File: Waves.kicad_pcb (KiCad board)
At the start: 2 copper layers, 49.8 x 106.5 mm, 154 parts, among them J1 AudioJack2_SwitchT, J10 AudioJack2_SwitchT, J11 Conn_01x04_Male, J12 Conn_01x04_Male, J13 AudioJack2_SwitchT, J14 AudioJack2_SwitchT, J15 Conn_02x05_Odd_Even, J2 AudioJack2_SwitchT, J3 AudioJack2_SwitchT, J4 AudioJack2_SwitchT, J5 AudioJack2_SwitchT, J6 AudioJack2_SwitchT, J7 AudioJack2_SwitchT, J8 AudioJack2_SwitchT, J9 AudioJack2_SwitchT, Q1 BC847, Q2 BC847, Q3 BC847, Q4 BC847, Q5 BC847, Q6 BC847, SW1 SW_Push, SW2 Rotary_Encoder_Switch, SW3 SW_Push_LED, SW4 SW_Push_LED, SW5 SW_Push_LED, SW6 SW_Push_LED, U1 STM32G431, U2 AT25xxx, U3 IPS240x240, U4 PCM5100, U5 TL072, U6 LM1117-3.3, U7 LM1117-3.3, U8 MCP6004, U9 MCP6004, Y1 8MHz

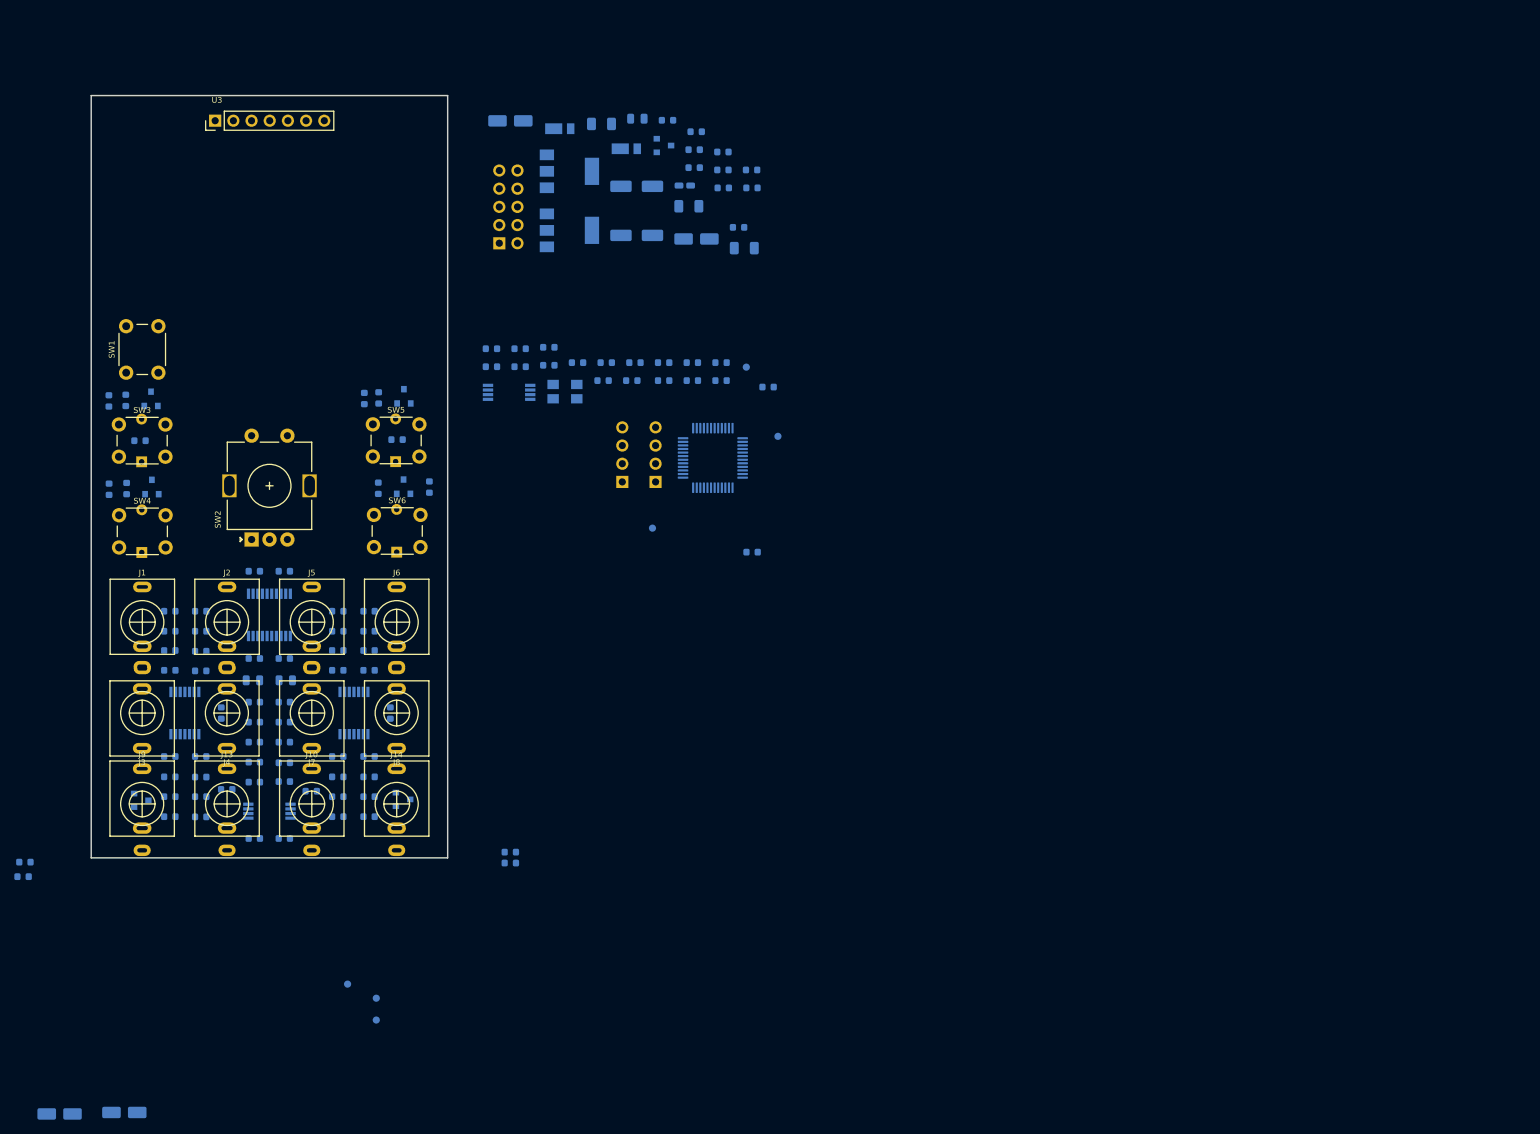
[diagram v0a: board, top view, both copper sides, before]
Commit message: Changed regulators and laid out power components.
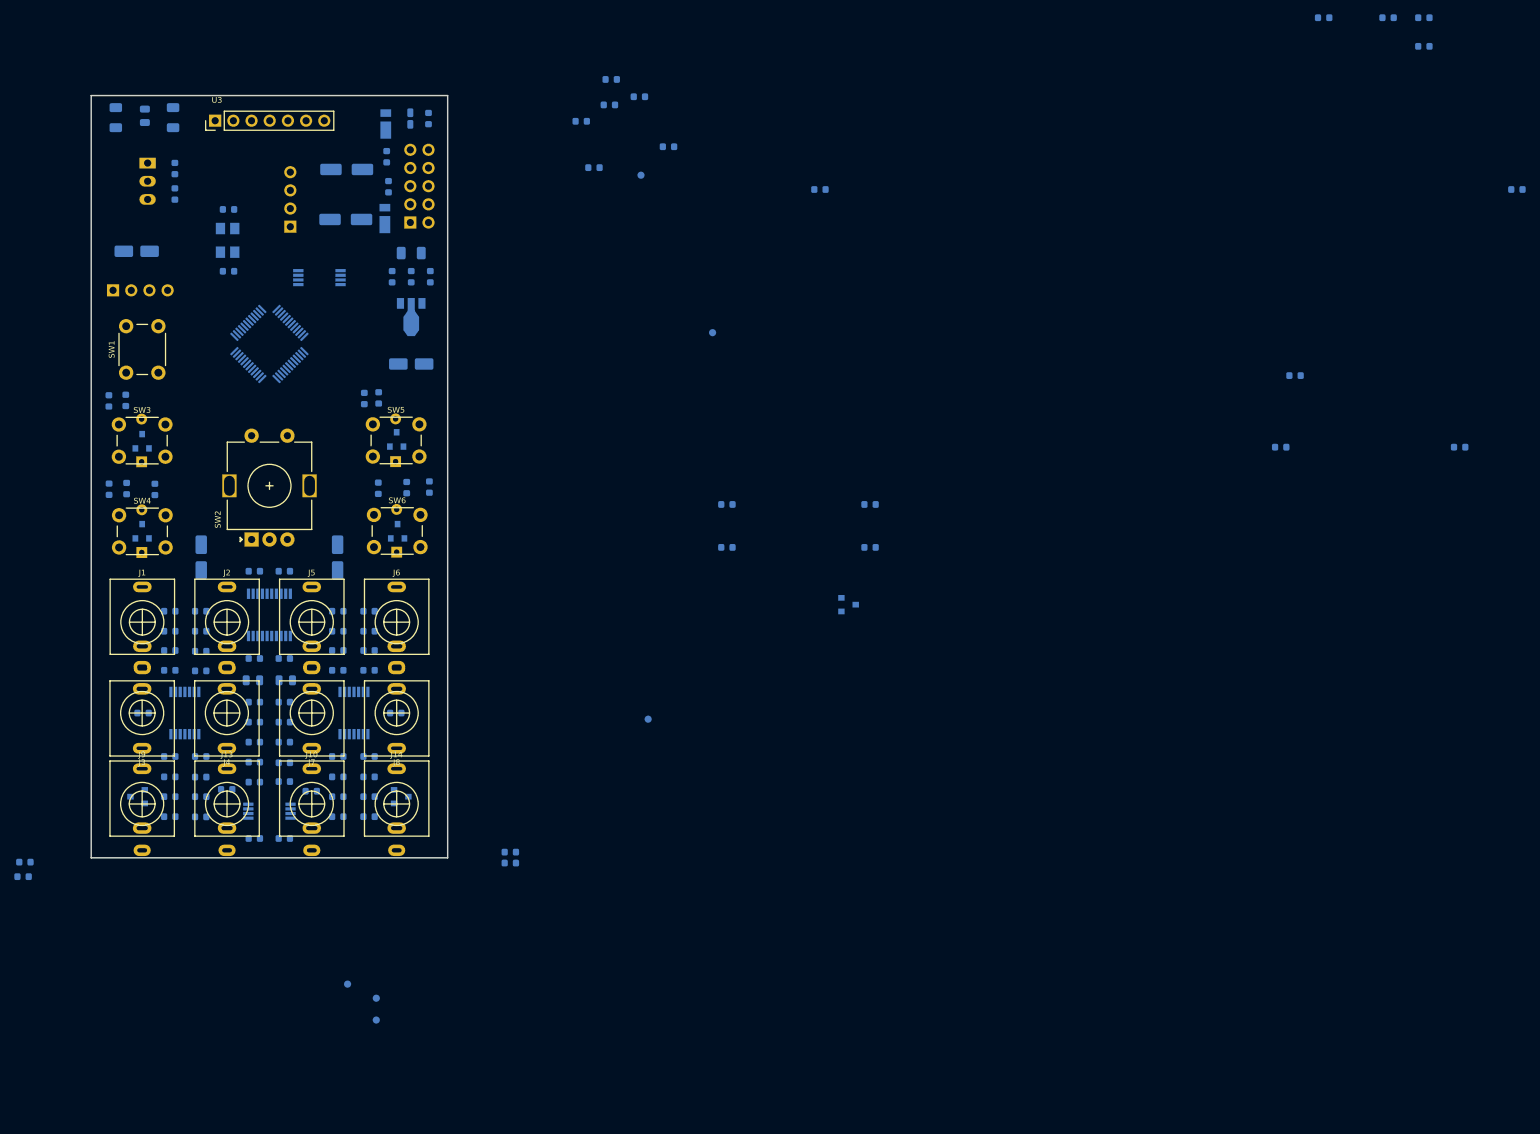
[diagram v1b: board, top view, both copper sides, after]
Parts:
- U6: value LM1117-3.3 -> R-78E3.3-0.5; footprint Package_TO_SOT_SMD:SOT-223-3_TabPin2 -> Converter_DCDC:Converter_DCDC_RECOM_R-78E-0.5_THT
- U7: value LM1117-3.3 -> LD2981ABU33TR; footprint Package_TO_SOT_SMD:SOT-223-3_TabPin2 -> Package_TO_SOT_SMD:SOT-89-3
- moved C13 126.1 mm to (274.2, 37.5)
- moved R6 121.6 mm to (301.2, 61.5)
- moved R4 113.0 mm to (288.2, 37.5)
- moved R3 108.7 mm to (288.2, 41.5)
- moved C42 105.3 mm to (293.2, 97.5)
- moved R9 104.9 mm to (283.2, 37.5)
- moved R19 87.0 mm to (268.2, 97.5)
- moved C17 83.0 mm to (136.4, 112.9), turned to 90 degrees
- moved C22 80.2 mm to (117.3, 112.9), turned to 90 degrees
- moved R5 79.8 mm to (270.2, 87.5)
- moved C40 78.2 mm to (108.3, 70.1), turned to 180 degrees
- moved J11 76.0 mm to (105.0, 75.6), turned to 270 degrees
- moved C31 73.1 mm to (113.4, 51.4), turned to 270 degrees
- moved C36 73.0 mm to (113.7, 58.5), turned to 270 degrees
- moved C38 69.6 mm to (113.7, 62.1), turned to 90 degrees
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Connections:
- U6 pad 1: GND -> Net-(C34-Pad1)
- U6 pad 2: +3V3 -> GND
- U6 pad 3: Net-(C34-Pad1) -> +3V3
- U7 pad 1: GND -> +3.3VA
- U7 pad 2: +3.3VA -> GND

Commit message: First pass complete layout.
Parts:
- removed TP4, TP5, TP6: TestPoint, TestPoint:TestPoint_Pad_D1.0mm
- moved R6 185.1 mm to (117.4, 84.3), turned to 180 degrees
- moved R4 174.1 mm to (116.6, 67.1), turned to 90 degrees
- moved R3 172.4 mm to (116.6, 58.7), turned to 90 degrees
- moved R5 161.1 mm to (109.1, 82.7)
- moved C13 158.9 mm to (124.0, 89.2), turned to 180 degrees
- moved C42 157.4 mm to (135.9, 91.4)
- moved R9 157.2 mm to (127.0, 55.5), turned to 270 degrees
- moved R19 132.3 mm to (135.9, 94.2), turned to 180 degrees
- moved C15 98.8 mm to (117.5, 78.9), turned to 180 degrees
- moved C16 97.8 mm to (117.5, 76.1), turned to 180 degrees
- moved C4 84.2 mm to (109.1, 85.1), turned to 180 degrees
- moved C14 79.1 mm to (124.7, 63.8), turned to 90 degrees
- moved D4 78.6 mm to (135.9, 87.6), turned to 90 degrees
- moved TP2 77.2 mm to (132.8, 134.6)
- moved C8 69.6 mm to (124.0, 91.9), turned to 180 degrees
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- renumbered C15 to C14, C14 to C15
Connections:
- C14 pad 1: +3.3VA -> +3V3
- R1 pad 1: +3.3VA -> +3V3
- R7 pad 1: +3.3VA -> +3V3

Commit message: Ground plane and keep-out for jacks.
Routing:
- added copper zone on In2.Cu, net GND
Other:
- copper layers 2 -> 4
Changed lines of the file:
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@@
   (layers
     (0 F.Cu signal)
+    (1 In1.Cu mixed)
+    (2 In2.Cu power)
     (31 B.Cu signal)
     (32 B.Adhes user)
@@
   (gr_line (start 151.775 154.849999) (end 151.775 48.349999) (layer Edge.Cuts) (width 0.2))
   (gr_line (start 101.974999 154.849999) (end 151.775 154.849999) (layer Edge.Cuts) (width 0.2))
+  (zone (net 75) (net_name GND) (layer In2.Cu) (hatch edge 0.508)
+    (connect_pads (clearance 0.508))
+    (min_thickness 0.254)
+    (fill yes (arc_segments 32) (thermal_gap 0.508) (thermal_bridge_width 0.508))
+    (polygon
+      (pts
+        (xy 101.981 48.387) (xy 151.765 48.387) (xy 151.765 154.813) (xy 101.981 154.813)
+      )
+    )
+  )
+  (zone (net 0) (net_name "") (layer F.Cu) (hatch edge 0.508)
+    (connect_pads (clearance 0.508))
+    (min_thickness 0.254)
+    (keepout (tracks not_allowed) (vias not_allowed) (copperpour not_allowed))
+    (fill (arc_segments 32) (thermal_gap 0.508) (thermal_bridge_width 0.508))
+    (polygon
+      (pts
+        (xy 144.653 120.142) (xy 143.891 120.269) (xy 143.256 120.777) (xy 142.875 121.539) (xy 142.875 122.301)
+        (xy 143.129 122.936) (xy 143.637 123.444) (xy 144.399 123.698) (xy 145.034 123.698) (xy 145.669 123.444)
+        (xy 146.177 122.936) (xy 146.431 122.301) (xy 146.431 121.539) (xy 146.177 120.904) (xy 145.796 120.523)
+        (xy 145.415 120.269) (xy 144.907 120.142)
+      )
+    )
+  )
+  (zone (net 0) (net_name "") (layer F.Cu) (hatch edge 0.508)
+    (connect_pads (clearance 0.508))
+    (min_thickness 0.254)
+    (keepout (tracks not_allowed) (vias not_allowed) (copperpour not_allowed))
+    (fill (arc_segments 32) (thermal_gap 0.508) (thermal_bridge_width 0.508))
+    (polygon
+      (pts
+        (xy 144.653 132.842) (xy 143.891 132.969) (xy 143.256 133.477) (xy 142.875 134.239) (xy 142.875 135.001)
+        (xy 143.129 135.636) (xy 143.637 136.144) (xy 144.399 136.398) (xy 145.034 136.398) (xy 145.669 136.144)
+        (xy 146.177 135.636) (xy 146.431 135.001) (xy 146.431 134.239) (xy 146.177 133.604) (xy 145.796 133.223)
+        (xy 145.415 132.969) (xy 144.907 132.842)
+      )
+    )
+  )
+  (zone (net 0) (net_name "") (layer F.Cu) (hatch edge 0.508)
+    (connect_pads (clearance 0.508))
+    (min_thickness 0.254)
+    (keepout (tracks not_allowed) (vias not_allowed) (copperpour not_allowed))
+    (fill (arc_segments 32) (thermal_gap 0.508) (thermal_bridge_width 0.508))
+    (polygon
+      (pts
+        (xy 144.653 145.542) (xy 143.891 145.669) (xy 143.256 146.177) (xy 142.875 146.939) (xy 142.875 147.701)
+        (xy 143.129 148.336) (xy 143.637 148.844) (xy 144.399 149.098) (xy 145.034 149.098) (xy 145.669 148.844)
+        (xy 146.177 148.336) (xy 146.431 147.701) (xy 146.431 146.939) (xy 146.177 146.304) (xy 145.796 145.923)
+        (xy 145.415 145.669) (xy 144.907 145.542)
+      )
+    )
+  )
+  (zone (net 0) (net_name "") (layer F.Cu) (hatch edge 0.508)
+    (connect_pads (clearance 0.508))
+    (min_thickness 0.254)
+    (keepout (tracks not_allowed) (vias not_allowed) (copperpour not_allowed))
+    (fill (arc_segments 32) (thermal_gap 0.508) (thermal_bridge_width 0.508))
+    (polygon
+      (pts
+        (xy 132.7785 145.542) (xy 132.0165 145.669) (xy 131.3815 146.177) (xy 131.0005 146.939) (xy 131.0005 147.701)
+        (xy 131.2545 148.336) (xy 131.7625 148.844) (xy 132.5245 149.098) (xy 133.1595 149.098) (xy 133.7945 148.844)
+        (xy 134.3025 148.336) (xy 134.5565 147.701) (xy 134.5565 146.939) (xy 134.3025 146.304) (xy 133.9215 145.923)
+        (xy 133.5405 145.669) (xy 133.0325 145.542)
+      )
+    )
+  )
+  (zone (net 0) (net_name "") (layer F.Cu) (hatch edge 0.508)
+    (connect_pads (clearance 0.508))
+    (min_thickness 0.254)
+    (keepout (tracks not_allowed) (vias not_allowed) (copperpour not_allowed))
+    (fill (arc_segments 32) (thermal_gap 0.508) (thermal_bridge_width 0.508))
+    (polygon
+      (pts
+        (xy 120.9675 145.542) (xy 120.2055 145.669) (xy 119.5705 146.177) (xy 119.1895 146.939) (xy 119.1895 147.701)
+        (xy 119.4435 148.336) (xy 119.9515 148.844) (xy 120.7135 149.098) (xy 121.3485 149.098) (xy 121.9835 148.844)
+        (xy 122.4915 148.336) (xy 122.7455 147.701) (xy 122.7455 146.939) (xy 122.4915 146.304) (xy 122.1105 145.923)
+        (xy 121.7295 145.669) (xy 121.2215 145.542)
+      )
+    )
+  )
+  (zone (net 0) (net_name "") (layer F.Cu) (hatch edge 0.508)
+    (connect_pads (clearance 0.508))
+    (min_thickness 0.254)
+    (keepout (tracks not_allowed) (vias not_allowed) (copperpour not_allowed))
+    (fill (arc_segments 32) (thermal_gap 0.508) (thermal_bridge_width 0.508))
+    (polygon
+      (pts
+        (xy 109.093 145.542) (xy 108.331 145.669) (xy 107.696 146.177) (xy 107.315 146.939) (xy 107.315 147.701)
+        (xy 107.569 148.336) (xy 108.077 148.844) (xy 108.839 149.098) (xy 109.474 149.098) (xy 110.109 148.844)
+        (xy 110.617 148.336) (xy 110.871 147.701) (xy 110.871 146.939) (xy 110.617 146.304) (xy 110.236 145.923)
+        (xy 109.855 145.669) (xy 109.347 145.542)
+      )
+    )
+  )
+  (zone (net 0) (net_name "") (layer F.Cu) (hatch edge 0.508)
+    (connect_pads (clearance 0.508))
+    (min_thickness 0.254)
+    (keepout (tracks not_allowed) (vias not_allowed) (copperpour not_allowed))
+    (fill (arc_segments 32) (thermal_gap 0.508) (thermal_bridge_width 0.508))
+    (polygon
+      (pts
+        (xy 109.093 132.842) (xy 108.331 132.969) (xy 107.696 133.477) (xy 107.315 134.239) (xy 107.315 135.001)
+        (xy 107.569 135.636) (xy 108.077 136.144) (xy 108.839 136.398) (xy 109.474 136.398) (xy 110.109 136.144)
+        (xy 110.617 135.636) (xy 110.871 135.001) (xy 110.871 134.239) (xy 110.617 133.604) (xy 110.236 133.223)
+        (xy 109.855 132.969) (xy 109.347 132.842)
+      )
+    )
+  )
+  (zone (net 0) (net_name "") (layer F.Cu) (hatch edge 0.508)
+    (connect_pads (clearance 0.508))
+    (min_thickness 0.254)
+    (keepout (tracks not_allowed) (vias not_allowed) (copperpour not_allowed))
+    (fill (arc_segments 32) (thermal_gap 0.508) (thermal_bridge_width 0.508))
+    (polygon
+      (pts
+        (xy 109.093 120.142) (xy 108.331 120.269) (xy 107.696 120.777) (xy 107.315 121.539) (xy 107.315 122.301)
+        (xy 107.569 122.936) (xy 108.077 123.444) (xy 108.839 123.698) (xy 109.474 123.698) (xy 110.109 123.444)
+        (xy 110.617 122.936) (xy 110.871 122.301) (xy 110.871 121.539) (xy 110.617 120.904) (xy 110.236 120.523)
+        (xy 109.855 120.269) (xy 109.347 120.142)
+      )
+    )
+  )
+  (zone (net 0) (net_name "") (layer F.Cu) (hatch edge 0.508)
+    (connect_pads (clearance 0.508))
+    (min_thickness 0.254)
+    (keepout (tracks not_allowed) (vias not_allowed) (copperpour not_allowed))
+    (fill (arc_segments 32) (thermal_gap 0.508) (thermal_bridge_width 0.508))
+    (polygon
+      (pts
+        (xy 120.9675 120.142) (xy 120.2055 120.269) (xy 119.5705 120.777) (xy 119.1895 121.539) (xy 119.1895 122.301)
+        (xy 119.4435 122.936) (xy 119.9515 123.444) (xy 120.7135 123.698) (xy 121.3485 123.698) (xy 121.9835 123.444)
+        (xy 122.4915 122.936) (xy 122.7455 122.301) (xy 122.7455 121.539) (xy 122.4915 120.904) (xy 122.1105 120.523)
+        (xy 121.7295 120.269) (xy 121.2215 120.142)
+      )
+    )
+  )
+  (zone (net 0) (net_name "") (layer F.Cu) (hatch edge 0.508)
+    (connect_pads (clearance 0.508))
+    (min_thickness 0.254)
+    (keepout (tracks not_allowed) (vias not_allowed) (copperpour not_allowed))
+    (fill (arc_segments 32) (thermal_gap 0.508) (thermal_bridge_width 0.508))
+    (polygon
+      (pts
+        (xy 132.7785 120.142) (xy 132.0165 120.269) (xy 131.3815 120.777) (xy 131.0005 121.539) (xy 131.0005 122.301)
+        (xy 131.2545 122.936) (xy 131.7625 123.444) (xy 132.5245 123.698) (xy 133.1595 123.698) (xy 133.7945 123.444)
+        (xy 134.3025 122.936) (xy 134.5565 122.301) (xy 134.5565 121.539) (xy 134.3025 120.904) (xy 133.9215 120.523)
+        (xy 133.5405 120.269) (xy 133.0325 120.142)
+      )
+    )
+  )
+  (zone (net 0) (net_name "") (layer F.Cu) (hatch edge 0.508)
+    (connect_pads (clearance 0.508))
+    (min_thickness 0.254)
+    (keepout (tracks not_allowed) (vias not_allowed) (copperpour not_allowed))
+    (fill (arc_segments 32) (thermal_gap 0.508) (thermal_bridge_width 0.508))
+    (polygon
+      (pts
+        (xy 132.7785 132.842) (xy 132.0165 132.969) (xy 131.3815 133.477) (xy 131.0005 134.239) (xy 131.0005 135.001)
+        (xy 131.2545 135.636) (xy 131.7625 136.144) (xy 132.5245 136.398) (xy 133.1595 136.398) (xy 133.7945 136.144)
+        (xy 134.3025 135.636) (xy 134.5565 135.001) (xy 134.5565 134.239) (xy 134.3025 133.604) (xy 133.9215 133.223)
+        (xy 133.5405 132.969) (xy 133.0325 132.842)
+      )
+    )
+  )
+  (zone (net 0) (net_name "") (layer F.Cu) (hatch edge 0.508)
+    (connect_pads (clearance 0.508))
+    (min_thickness 0.254)
+    (keepout (tracks not_allowed) (vias not_allowed) (copperpour not_allowed))
+    (fill (arc_segments 32) (thermal_gap 0.508) (thermal_bridge_width 0.508))
+    (polygon
+      (pts
+        (xy 120.904 132.842) (xy 120.142 132.969) (xy 119.507 133.477) (xy 119.126 134.239) (xy 119.126 135.001)
+        (xy 119.38 135.636) (xy 119.888 136.144) (xy 120.65 136.398) (xy 121.285 136.398) (xy 121.92 136.144)
+        (xy 122.428 135.636) (xy 122.682 135.001) (xy 122.682 134.239) (xy 122.428 133.604) (xy 122.047 133.223)
+        (xy 121.666 132.969) (xy 121.158 132.842)
+      )
+    )
+  )
 )

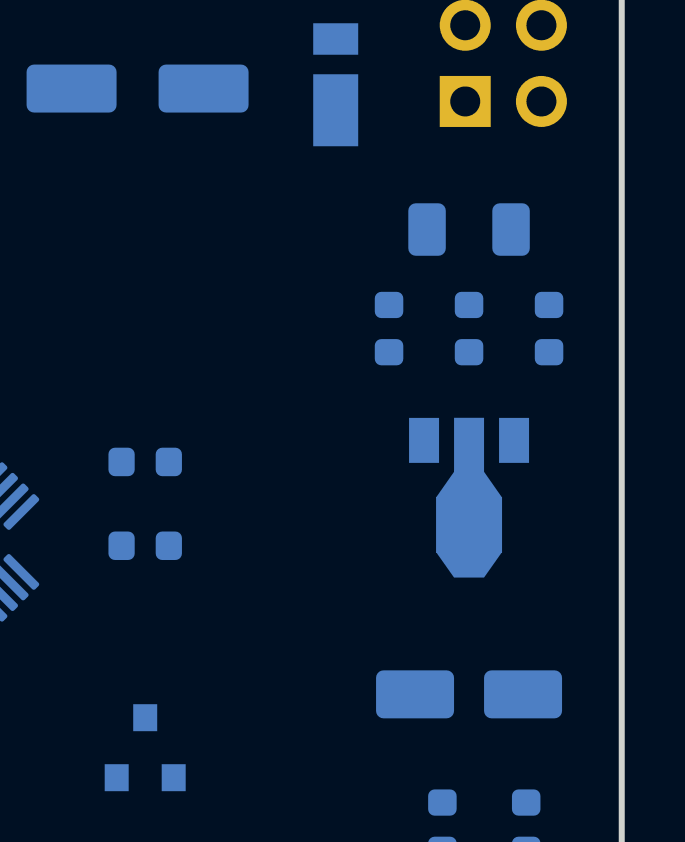
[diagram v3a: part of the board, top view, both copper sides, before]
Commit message: Heat-sink for analog supply.
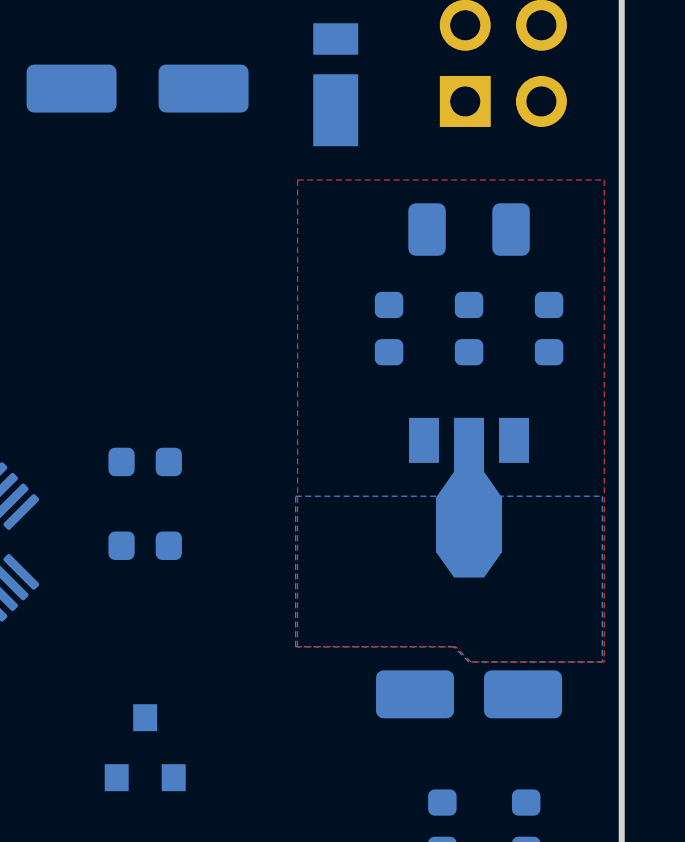
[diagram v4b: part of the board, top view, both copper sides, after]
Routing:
- added copper zone on B.Cu, net GND
- added copper zone on F.Cu, net GND
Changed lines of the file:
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@@
+    )
+  )
+  (zone (net 75) (net_name GND) (layer B.Cu) (hatch edge 0.508)
+    (connect_pads (clearance 0.508))
+    (min_thickness 0.254)
+    (fill yes (arc_segments 32) (thermal_gap 0.508) (thermal_bridge_width 0.508))
+    (polygon
+      (pts
+        (xy 147.6375 79.248) (xy 151.13 79.248) (xy 151.13 84.7725) (xy 146.685 84.7725) (xy 146.177 84.2645)
+        (xy 140.9065 84.2645) (xy 140.9065 79.248)
+      )
+    )
+  )
+  (zone (net 75) (net_name GND) (layer F.Cu) (hatch edge 0.508)
+    (connect_pads (clearance 0.508))
+    (min_thickness 0.254)
+    (fill yes (arc_segments 32) (thermal_gap 0.508) (thermal_bridge_width 0.508))
+    (polygon
+      (pts
+        (xy 151.1935 68.707) (xy 151.1935 84.7725) (xy 146.7485 84.7725) (xy 146.2405 84.2645) (xy 140.97 84.2645)
+        (xy 140.97 68.707)
+      )
     )
   )
